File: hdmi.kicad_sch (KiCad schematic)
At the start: 10 parts, among them J8 HDMI-A_HDMI-19PIN-043, U2 AP22615AWU-7

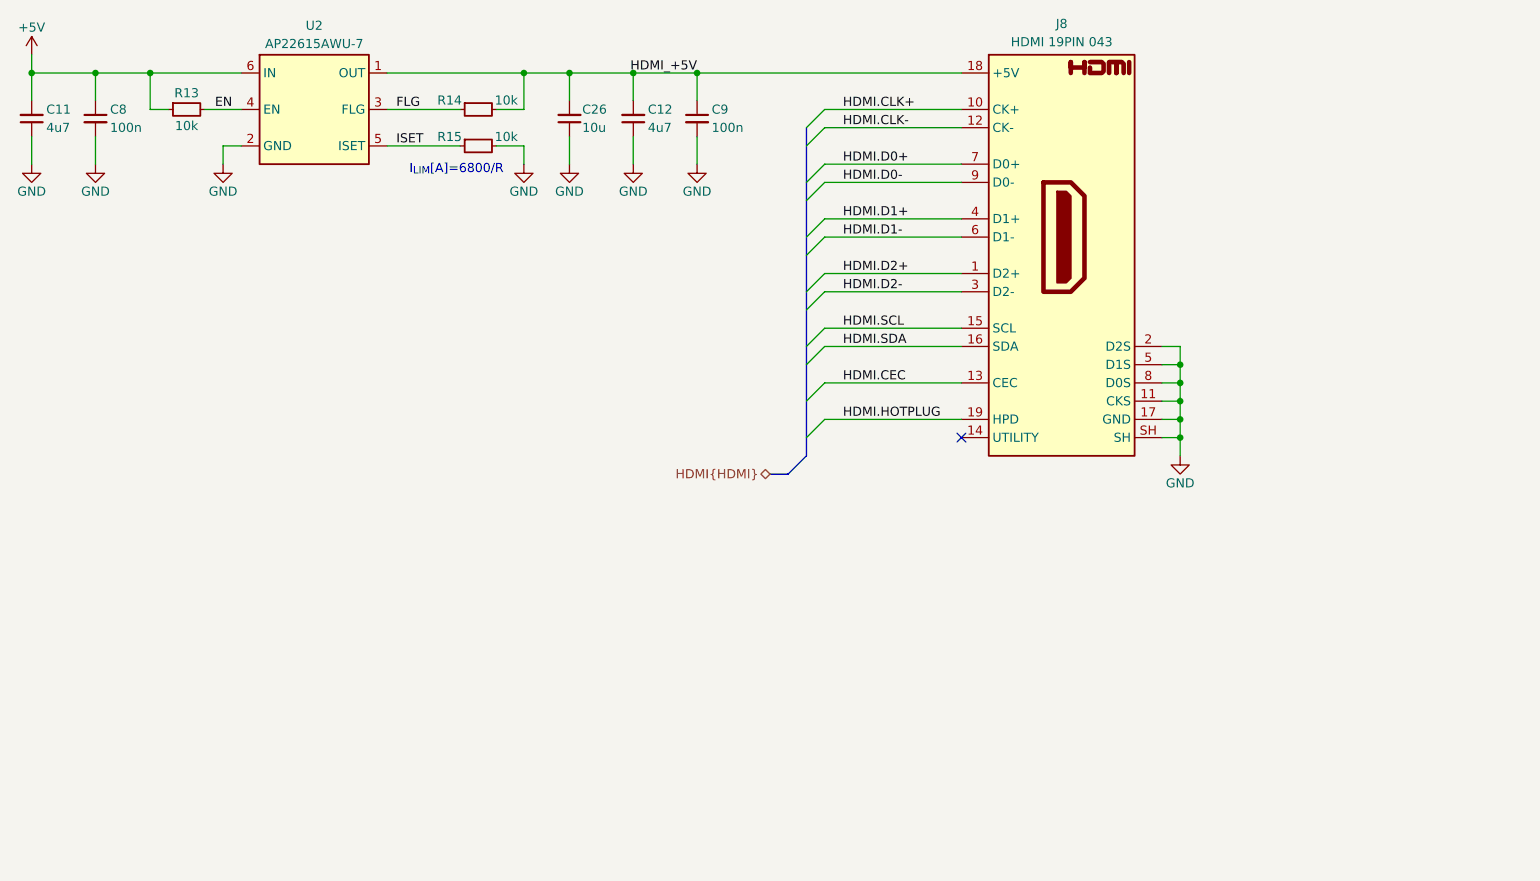
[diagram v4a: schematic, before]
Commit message: [#3] Add TVS, route HDMI and fanout ETH
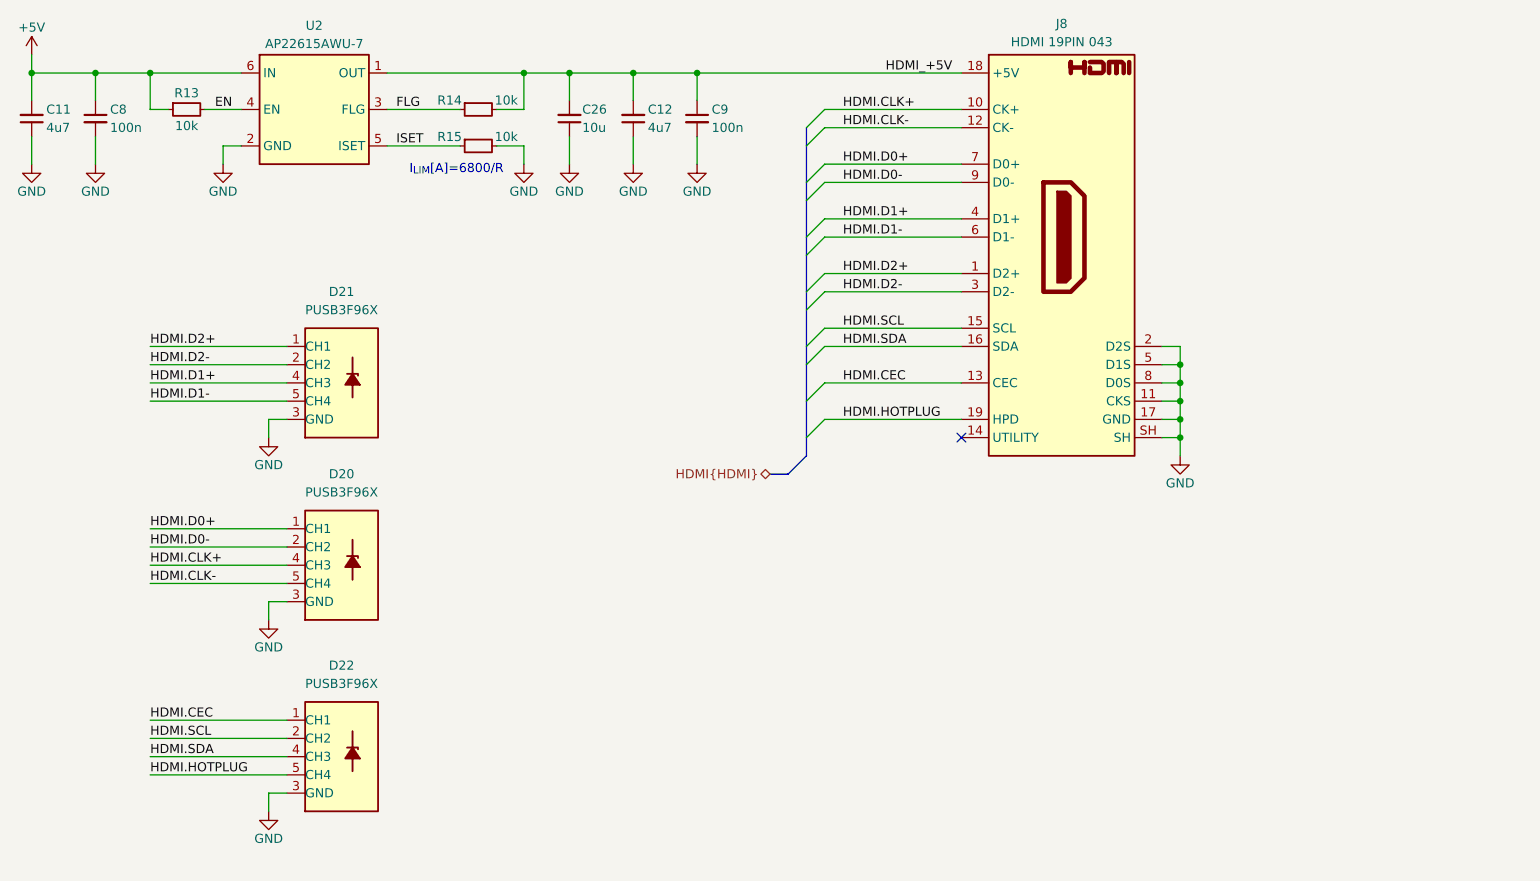
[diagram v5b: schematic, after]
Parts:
- added D20, D21, D22: PUSB3F96X, DW-footprints:SOT1176-1, symbol DW-TVS:PUSB3F96X
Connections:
- net GND: now also D20.3 (GND), D20.8 (GND), D21.3 (GND), D21.8 (GND), D22.3 (GND), D22.8 (GND)
- net HDMI.CEC: now also D22.1 (CH1), D22.10 (CH1)
- net HDMI.CLK+: now also D20.4 (CH3), D20.7 (CH3)
- net HDMI.CLK-: now also D20.5 (CH4), D20.6 (CH4)
- net HDMI.D0+: now also D20.1 (CH1), D20.10 (CH1)
- net HDMI.D0-: now also D20.2 (CH2), D20.9 (CH2)
- net HDMI.D1+: now also D21.4 (CH3), D21.7 (CH3)
- net HDMI.D1-: now also D21.5 (CH4), D21.6 (CH4)
- net HDMI.D2+: now also D21.1 (CH1), D21.10 (CH1)
- net HDMI.D2-: now also D21.2 (CH2), D21.9 (CH2)
- net HDMI.HOTPLUG: now also D22.5 (CH4), D22.6 (CH4)
- net HDMI.SCL: now also D22.2 (CH2), D22.9 (CH2)
- net HDMI.SDA: now also D22.4 (CH3), D22.7 (CH3)

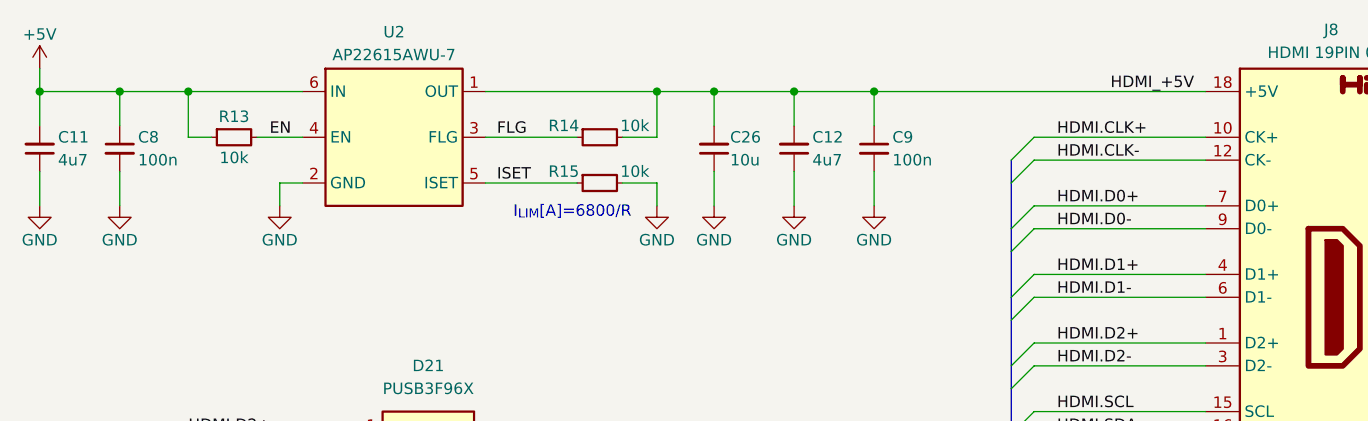
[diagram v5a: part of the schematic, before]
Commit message: [#3] Continue layout, minor schematic fixes, add power switch for CAN transceiver 5V rail
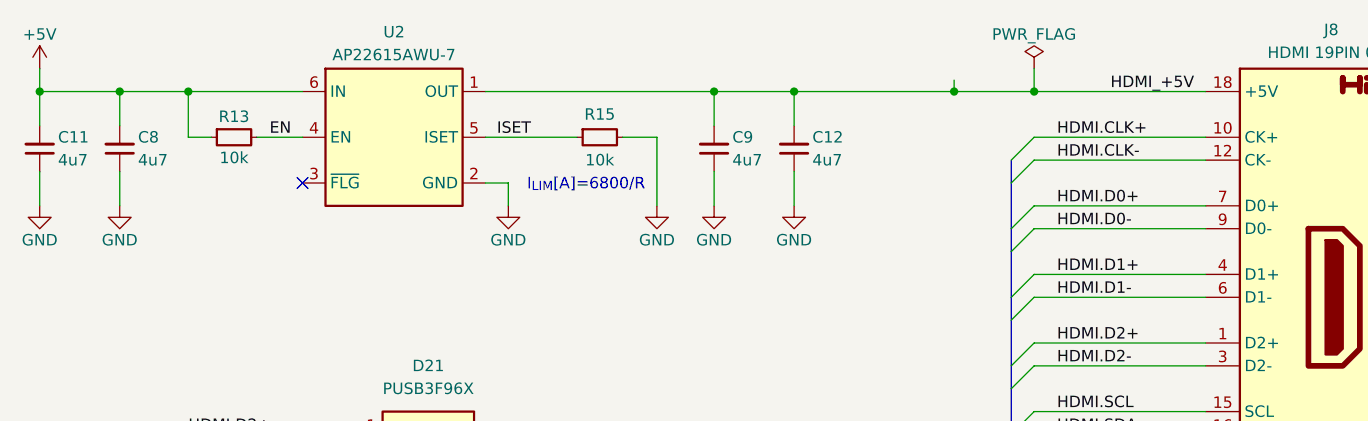
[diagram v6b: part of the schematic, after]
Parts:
- removed C26: C-10u-0603, DW-footprints:C_0603_1608Metric, symbol DW-capacitors:C-10u-0603
- removed C8, C9: C-100n-0402, DW-footprints:C_0402_1005Metric, symbol DW-capacitors:C-100n-0402
- removed R14: R-10k-0402, DW-footprints:R_0402_1005Metric, symbol DW-resistors:R-10k-0402
- added C8, C9: C-4u7-0402, DW-footprints:C_0402_1005Metric, symbol DW-capacitors:C-4u7-0402
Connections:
- net +5V: now also C8.2
- net GND: now also C8.1, C9.1
- net HDMI_+5V: now also C9.2
- net FLG: no longer names the net of U2.3 (~{FLG})
- no-connect marks 1 -> 2
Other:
- moved on the sheet: R15
